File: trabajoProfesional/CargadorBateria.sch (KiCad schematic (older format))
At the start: 0 parts

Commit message: Placa uno terminada!
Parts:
- added IC?: TS51231-QFNR, QFN50P300X300X100-17N-D, symbol TS51231-QFNR:TS51231-QFNR
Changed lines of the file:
@@
 Comment4 ""
 $EndDescr
+$Comp
+L TS51231-QFNR:TS51231-QFNR IC?
+U 1 1 5FFE6889
+P 3350 3100
+F 0 "IC?" H 4594 3046 50  0000 L CNN
+F 1 "TS51231-QFNR" H 4594 2955 50  0000 L CNN
+F 2 "QFN50P300X300X100-17N-D" H 4400 3600 50  0001 L CNN
+F 3 "https://www.semtech.com/uploads/documents/ts51231.pdf" H 4400 3500 50  0001 L CNN
+F 4 "Wireless Charging ICs High Efficiency Transmitter Driver" H 4400 3400 50  0001 L CNN "Description"
+F 5 "1" H 4400 3300 50  0001 L CNN "Height"
+F 6 "947-TS51231-QFNR" H 4400 3200 50  0001 L CNN "Mouser Part Number"
+F 7 "https://www.mouser.co.uk/ProductDetail/Semtech/TS51231-QFNR?qs=rBWM4%252BvDhIc266YipLkS3A%3D%3D" H 4400 3100 50  0001 L CNN "Mouser Price/Stock"
+F 8 "SEMTECH" H 4400 3000 50  0001 L CNN "Manufacturer_Name"
+F 9 "TS51231-QFNR" H 4400 2900 50  0001 L CNN "Manufacturer_Part_Number"
+	1    3350 3100
+	1    0    0    -1
+$EndComp
 $EndSCHEMATC

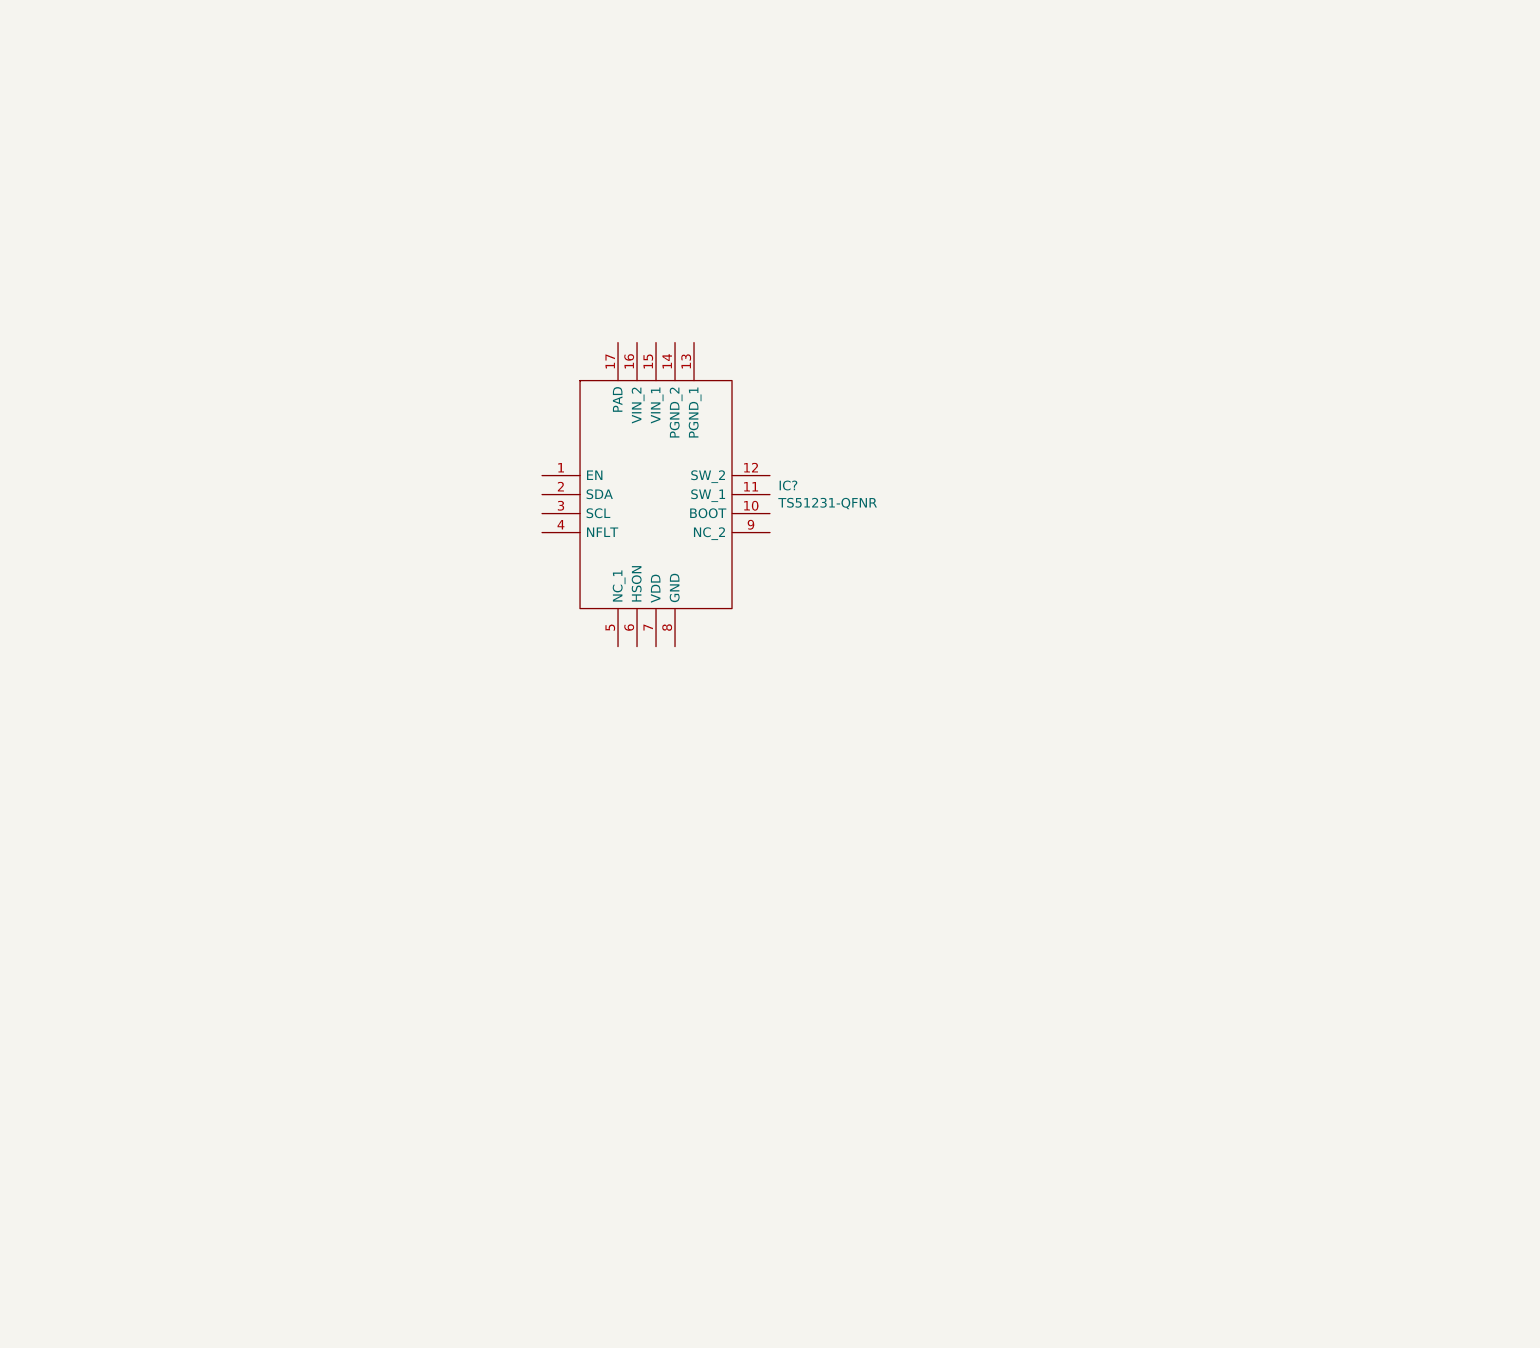
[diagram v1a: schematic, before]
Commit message: agregamos los dos circuitos que nos faltaban, cargador y centralizador
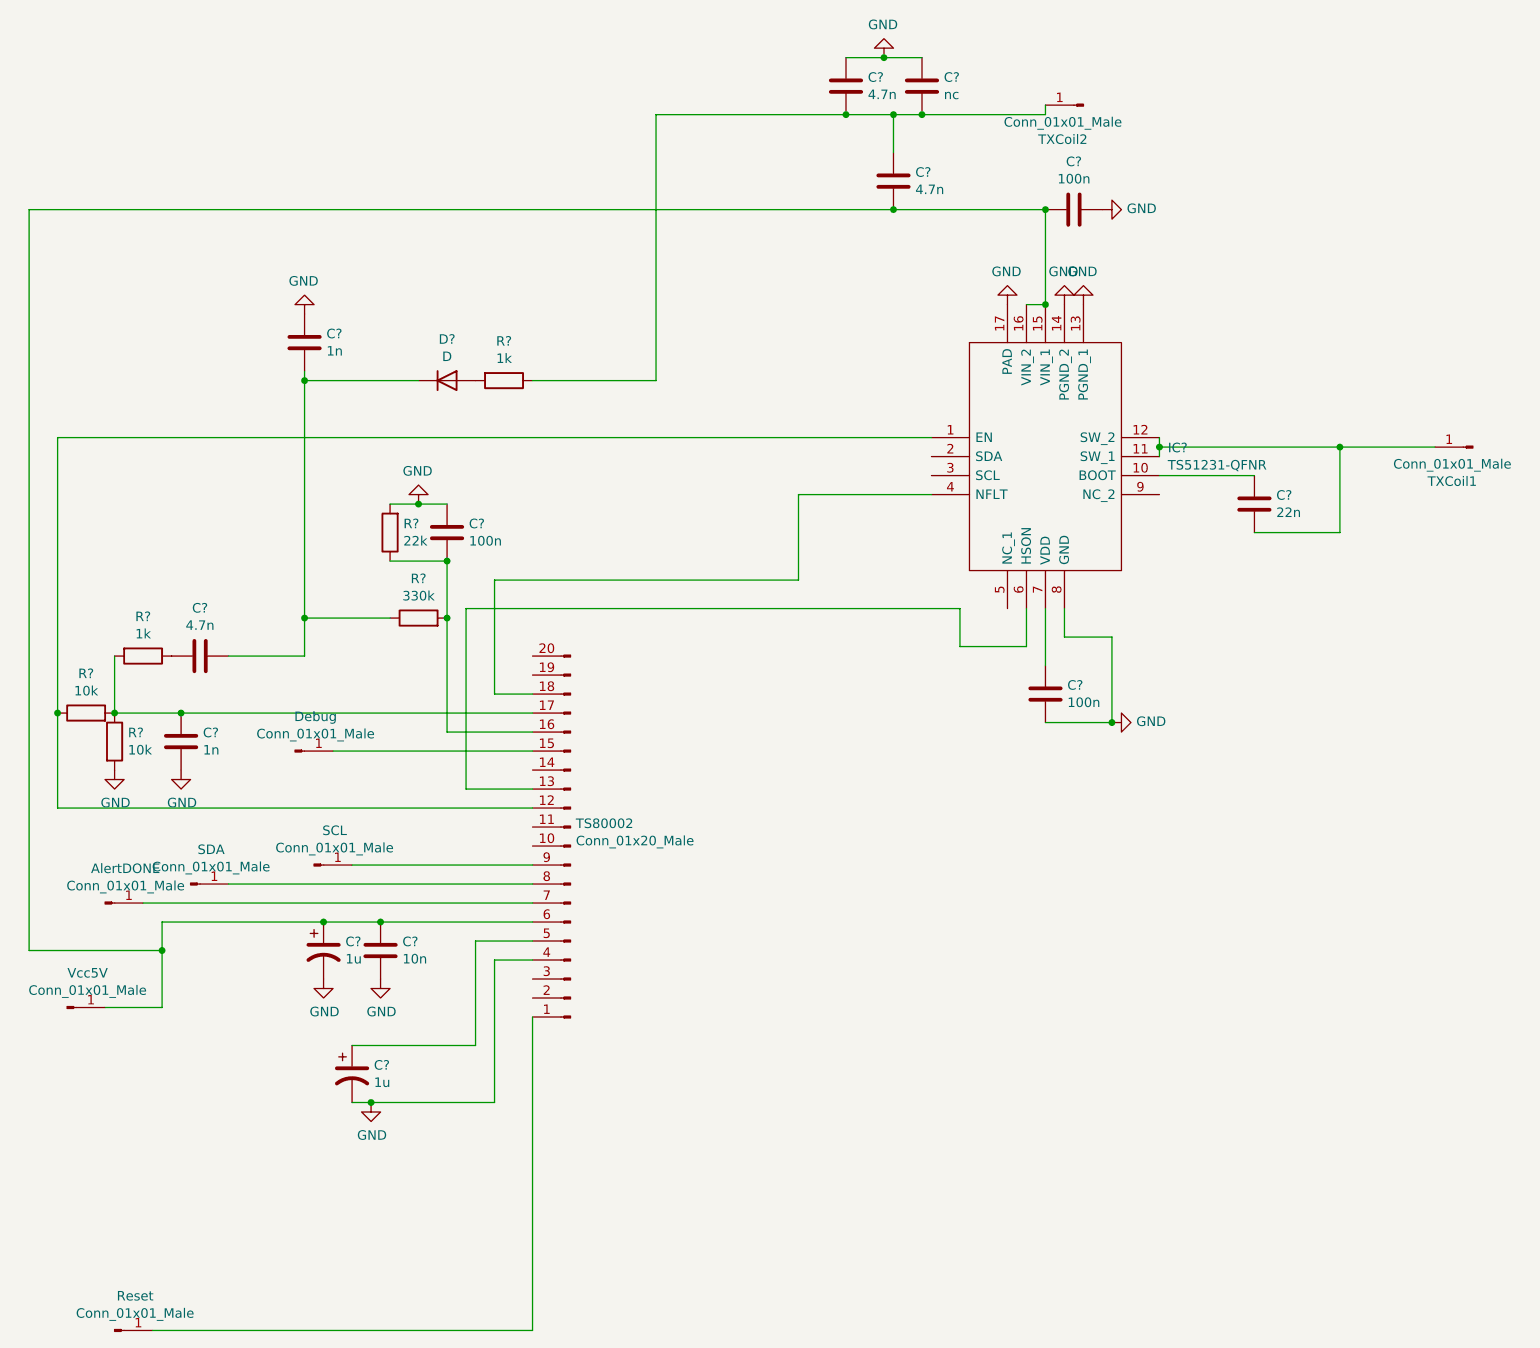
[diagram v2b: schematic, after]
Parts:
- added AlertDONE, Debug, Reset, SCL, SDA, TXCoil1, TXCoil2, Vcc5V: Conn_01x01_Male, symbol Connector:Conn_01x01_Male
- added C? (x2): 1u, symbol Device:CP1
- added C?: 10n, symbol Device:C
- added C? (x2): 1n, symbol Device:C
- added C? (x3): 4.7n, symbol Device:C
- added C? (x3): 100n, symbol Device:C
- added C?: 22n, symbol Device:C
- added C?: nc, symbol Device:C
- added D?: D, symbol Device:D
- added R? (x2): 10k, symbol Device:R
- added R? (x2): 1k, symbol Device:R
- added R?: 22k, symbol Device:R
- added R?: 330k, symbol Device:R
- added TS80002: Conn_01x20_Male, symbol Connector:Conn_01x20_Male
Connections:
- net at IC?.1 (EN): now also R?.1, TS80002.12 (Pin_12)
- net at IC?.10 (BOOT): now also C?.2
- net at IC?.11 (SW_1): now also IC?.12 (SW_2), C?.1, TXCoil1.1 (Pin_1)
- net GND: now reaches IC?.13 (PGND_1)
- net GND: now also IC?.14 (PGND_2), IC?.17 (PAD), IC?.8 (GND), C?.1, C?.2, C?.2, C?.2, C?.2, C?.2, C?.2, C?.2, C?.2, C?.2, R?.2, R?.2, TS80002.4 (Pin_4)
- net at IC?.15 (VIN_1): now also IC?.16 (VIN_2), C?.1, C?.1, C?.1, C?.2, TS80002.6 (Pin_6), Vcc5V.1 (Pin_1)
- net at IC?.4 (NFLT): now also TS80002.18 (Pin_18)
- net at IC?.6 (HSON): now also TS80002.13 (Pin_13)
- net at IC?.7 (VDD): now also C?.2
- new net: Reset.1 (Pin_1), TS80002.1 (Pin_1)
- new net: Debug.1 (Pin_1), TS80002.15 (Pin_15)
- new net: C?.1, R?.1, R?.2, TS80002.16 (Pin_16)
- new net: C?.1, R?.1, R?.2, R?.2, TS80002.17 (Pin_17)
- new net: C?.1, TS80002.5 (Pin_5)
- new net: AlertDONE.1 (Pin_1), TS80002.7 (Pin_7)
- new net: SDA.1 (Pin_1), TS80002.8 (Pin_8)
- new net: SCL.1 (Pin_1), TS80002.9 (Pin_9)
- new net: C?.2, R?.1
- new net: C?.1, C?.1, D?.1 (K), R?.1
- new net: D?.2 (A), R?.2
- new net: C?.1, C?.1, C?.1, R?.1, TXCoil2.1 (Pin_1)
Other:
- moved on the sheet: IC?

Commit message: el paso previo a agregar todos los componentes de las otras placas
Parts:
- AlertDONE1: renamed from AlertDONE; footprint (none) -> TestPoint:TestPoint_Pad_D3.0mm
- C10, C11: renamed from C?; footprint (none) -> Capacitor_SMD:CP_Elec_6.3x5.9
- C12, C13, C14, C15, C16, C17, C18, C19, C7, C8, C9: renamed from C?; footprint (none) -> Capacitor_SMD:C_0805_2012Metric
- D5: renamed from D?; footprint (none) -> Diode_SMD:D_0805_2012Metric
- Debug1: renamed from Debug; footprint (none) -> TestPoint:TestPoint_Pad_D3.0mm
- IC1: renamed from IC?; footprint QFN50P300X300X100-17N-D -> TS51231-QFNR:QFN50P300X300X100-17N-D
- R3, R4, R5, R6, R7, R8: renamed from R?; footprint (none) -> Resistor_SMD:R_0805_2012Metric
- Reset1: renamed from Reset; footprint (none) -> TestPoint:TestPoint_Pad_D4.0mm
- SCL1: renamed from SCL; footprint (none) -> TestPoint:TestPoint_Pad_D3.0mm
- SDA1: renamed from SDA; footprint (none) -> TestPoint:TestPoint_Pad_D3.0mm
- TS80002: footprint (none) -> QFN40P300X300X60-21N:QFN40P300X300X60-21N
- TXCoil1, TXCoil2: footprint (none) -> TestPoint:TestPoint_Pad_D4.0mm
- Vcc5V1: renamed from Vcc5V; footprint (none) -> TestPoint:TestPoint_Pad_D3.0mm
